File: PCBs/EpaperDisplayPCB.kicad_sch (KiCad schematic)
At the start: 25 parts, among them J1 Conn_01x12_FPC_0.5mm, J2 Conn_01x08, Q1 AO3404A, U1 ePaper-2.66

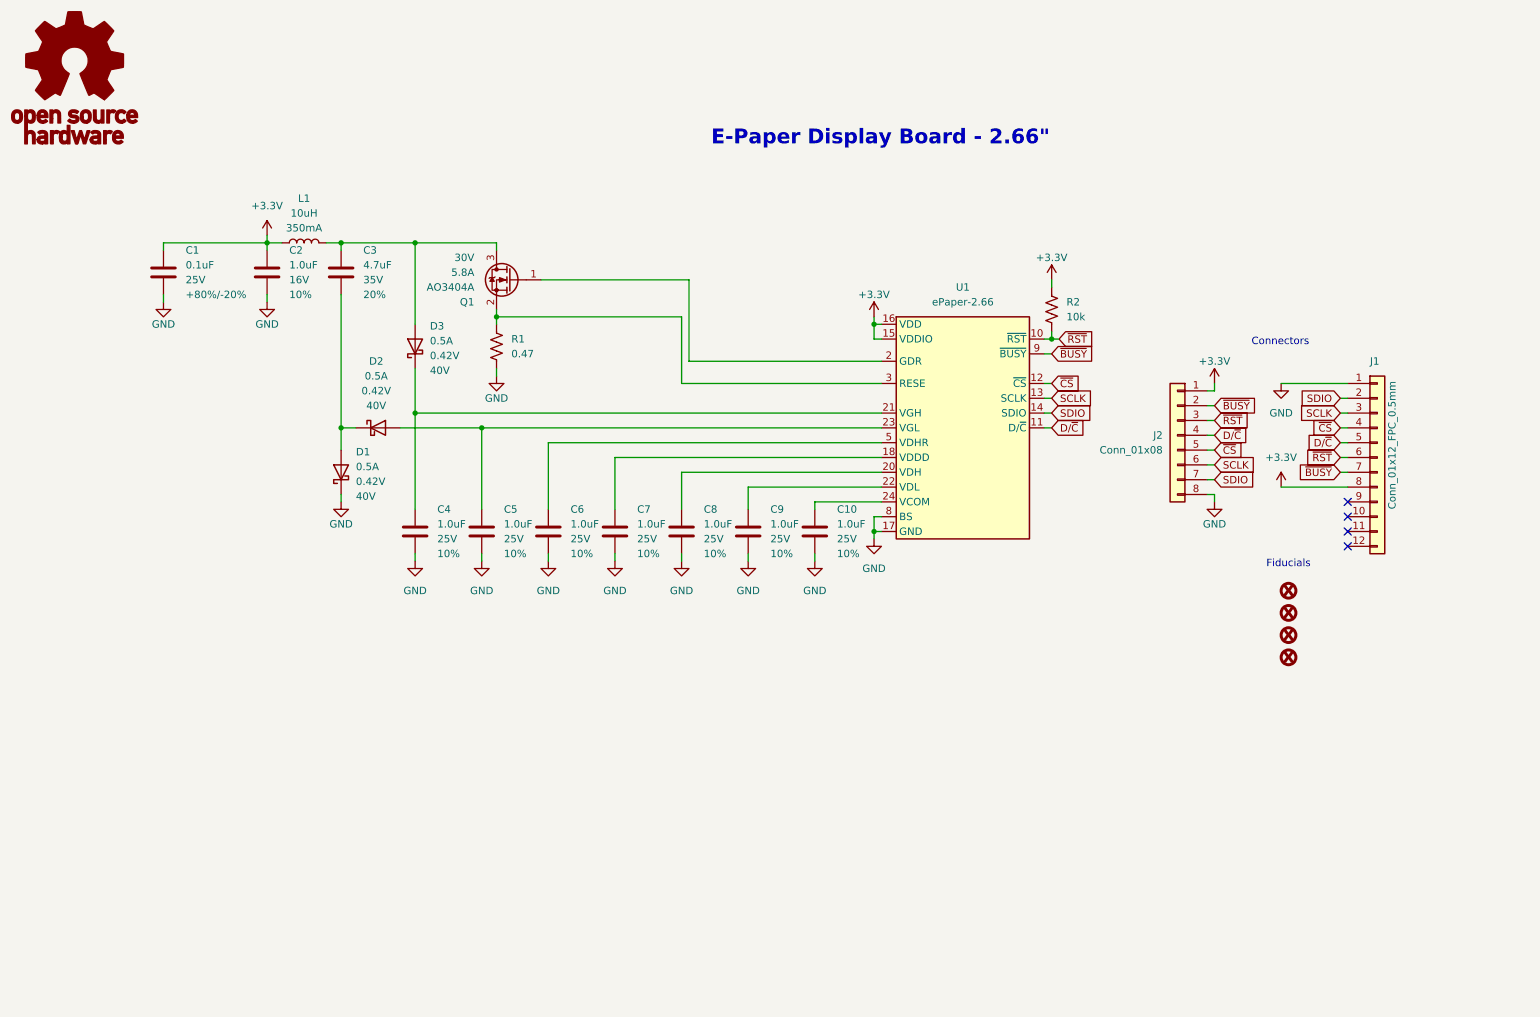
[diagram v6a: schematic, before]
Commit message: Screen and Main Board Updates
Updated Main board to Screen PCB connection, added accelerometer to Epaper display PCB. Removed GPIO 0 PB and replaced external Reset button with GPIO0 button.
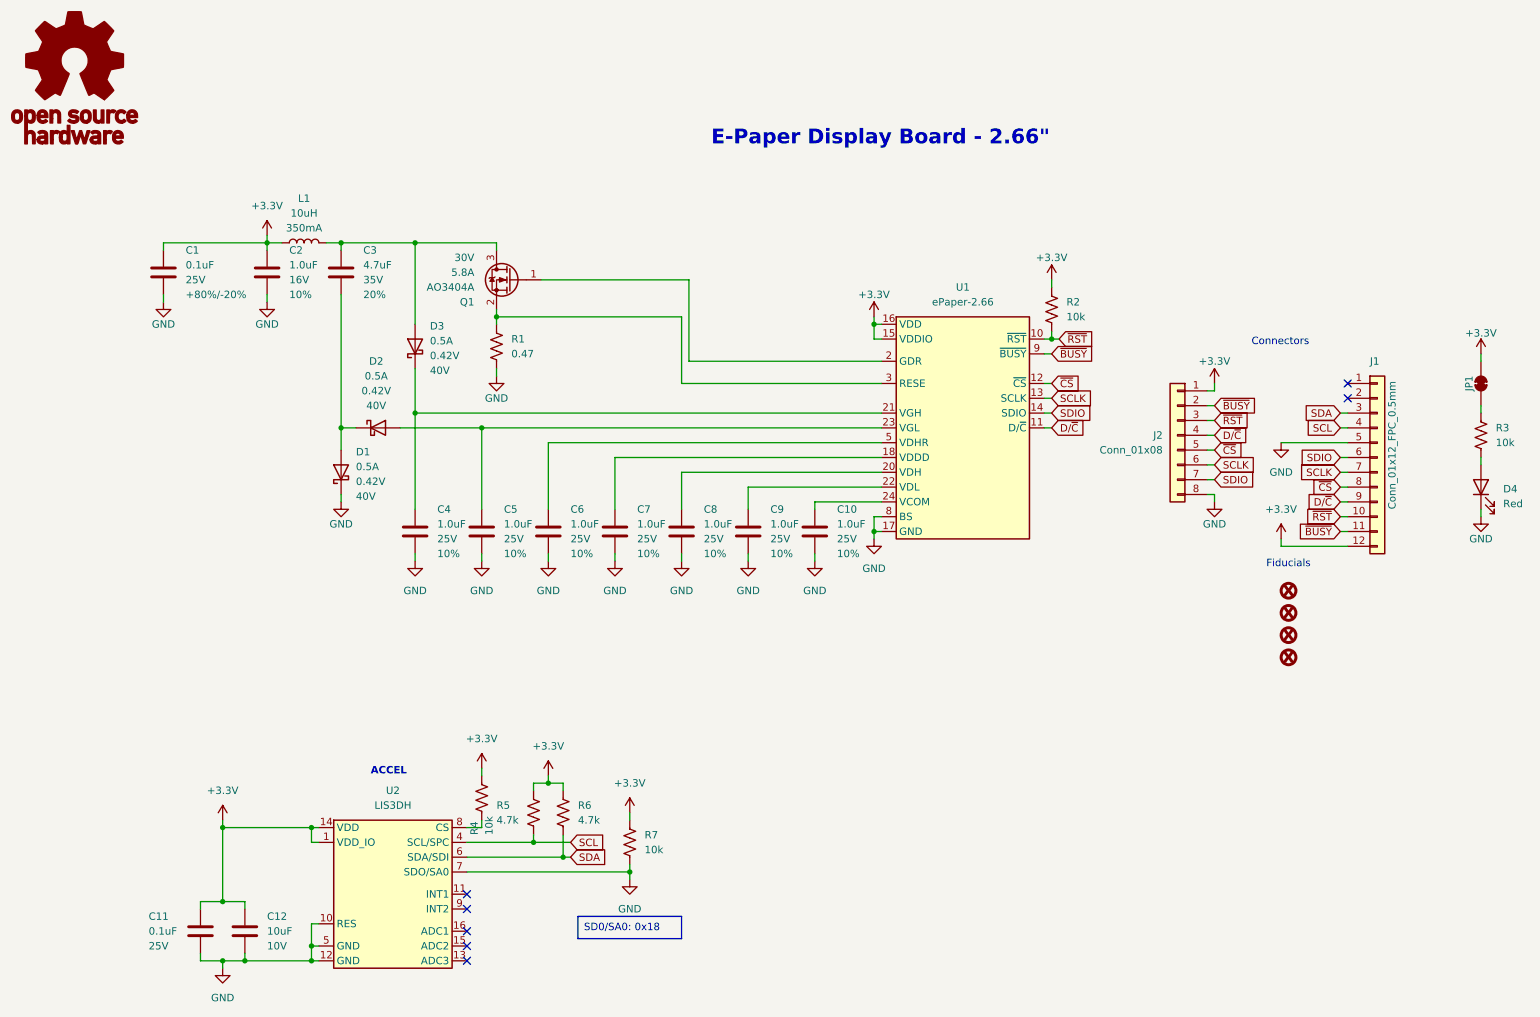
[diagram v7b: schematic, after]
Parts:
- added C11: 0.1uF, SparkFun-Capacitor:C_0603_1608Metric, symbol SparkFun-Capacitor:0.1uF_0603_25V_20%
- added C12: 10uF, SparkFun-Capacitor:C_0603_1608Metric, symbol SparkFun-Capacitor:10uF_0603_10V_20%
- added D4: Red, SparkFun-LED:LED_0603_1608Metric, symbol SparkFun-LED:LED_Red_0603
- added JP1: ~, SparkFun-Jumper:SMT-JUMPER_2_NC_TRACE_SILK, symbol SparkFun-Jumper:SolderJumper_2_Bridged
- added R3, R4, R7: 10k, SparkFun-Resistor:R_0603_1608Metric, symbol SparkFun-Resistor:10k_0603
- added R5, R6: 4.7k, SparkFun-Resistor:R_0603_1608Metric, symbol SparkFun-Resistor:4.7k_0603
- added U2: LIS3DH, Package_LGA:LGA-16_3x3mm_P0.5mm_LayoutBorder3x5y, symbol SparkFun-Sensor:LIS3DH
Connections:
- net +3.3V: now also J1.12 (Pin_12), C11.1, C12.1, JP1.2 (B), R4.2, R5.1, R6.1, R7.2, U2.1 (VDD_IO), U2.14 (VDD); no longer J1.8 (Pin_8)
- net D/~{C}: now also J1.9 (Pin_9); no longer J1.5 (Pin_5)
- net GND: now also J1.5 (Pin_5), C11.2, C12.2, D4.1 (K), R7.1, U2.10 (RES), U2.12 (GND), U2.5 (GND), U2.7 (SDO/SA0); no longer J1.1 (Pin_1)
- net SCLK: now also J1.7 (Pin_7); no longer J1.3 (Pin_3)
- net SDIO: now also J1.6 (Pin_6); no longer J1.2 (Pin_2)
- net ~{BUSY}: now also J1.11 (Pin_11); no longer J1.7 (Pin_7)
- net ~{CS}: now also J1.8 (Pin_8); no longer J1.4 (Pin_4)
- net ~{RST}: now also J1.10 (Pin_10); no longer J1.6 (Pin_6)
- new net: JP1.1 (A), R3.2
- new net: R4.1, U2.8 (CS)
- new net: D4.2 (A), R3.1
- new net SCL: J1.4 (Pin_4), R5.2, U2.4 (SCL/SPC)
- new net SDA: J1.3 (Pin_3), R6.2, U2.6 (SDA/SDI)
- no-connect marks 4 -> 7
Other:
- note added: "ACCEL"

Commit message: Adding updates From review
Fixed epaper to main board FPC connection.
Added fiducials to main board for stencil alignment purposes.
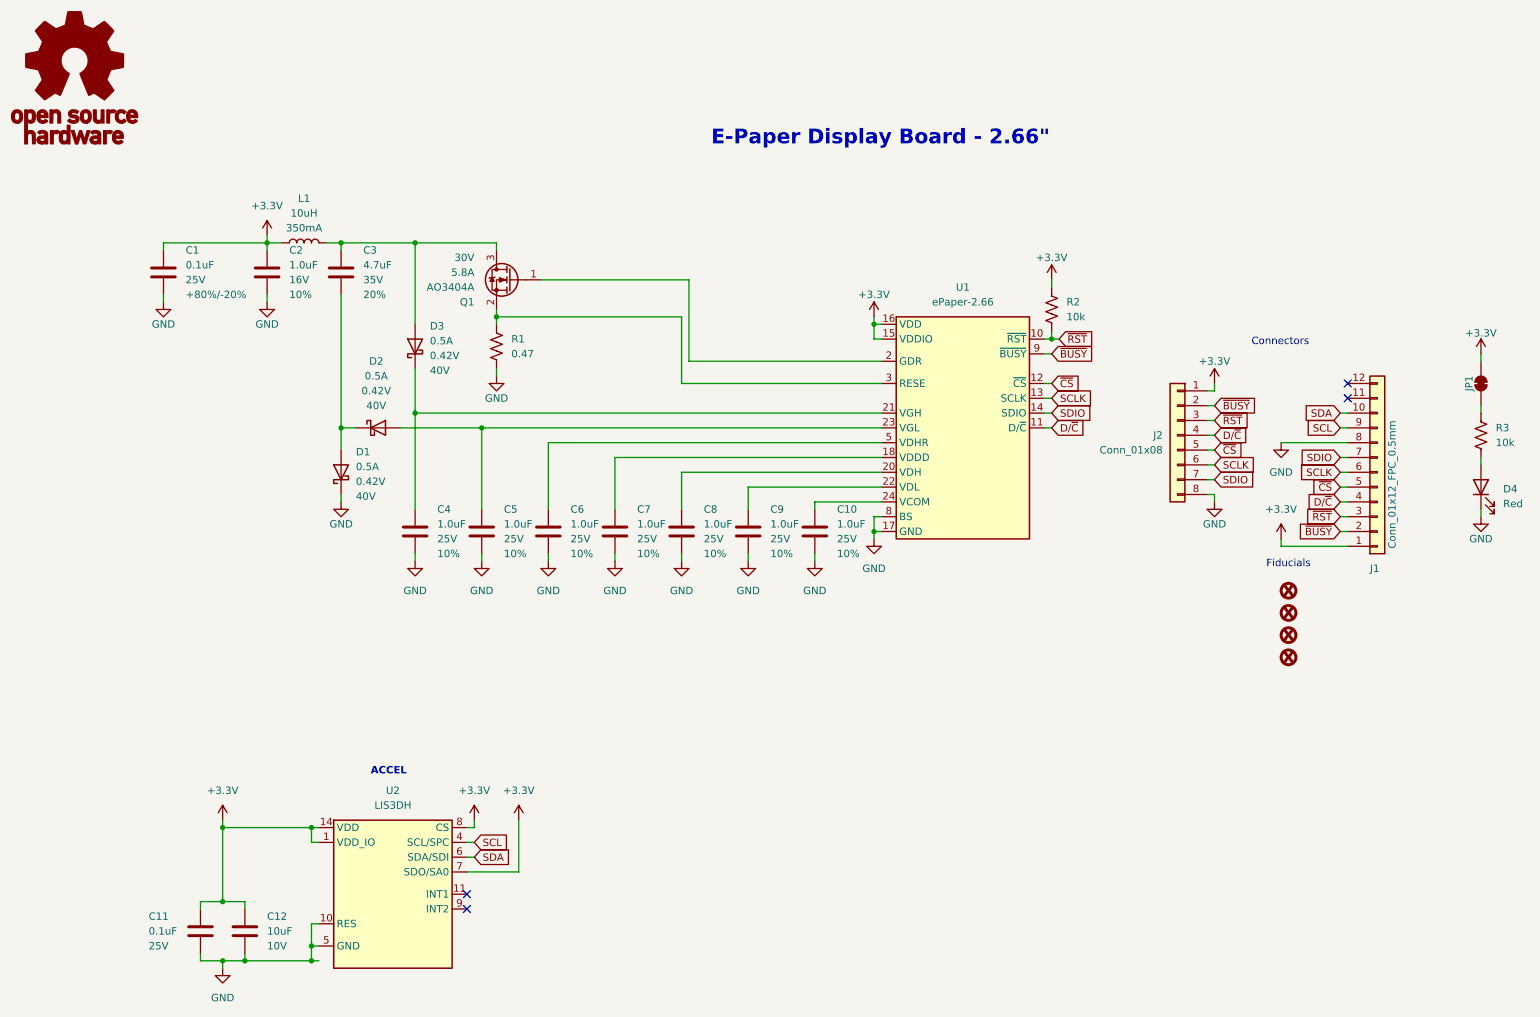
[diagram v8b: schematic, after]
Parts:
- removed R4, R7: 10k, SparkFun-Resistor:R_0603_1608Metric, symbol SparkFun-Resistor:10k_0603
- removed R5, R6: 4.7k, SparkFun-Resistor:R_0603_1608Metric, symbol SparkFun-Resistor:4.7k_0603
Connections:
- net +3.3V: now also J1.1 (Pin_1), U2.7 (SDO/SA0), U2.8 (CS); no longer J1.12 (Pin_12)
- net D/~{C}: now also J1.4 (Pin_4); no longer J1.9 (Pin_9)
- net GND: now also J1.8 (Pin_8); no longer J1.5 (Pin_5), U2.7 (SDO/SA0)
- net SCL: now also J1.9 (Pin_9); no longer J1.4 (Pin_4)
- net SCLK: now also J1.6 (Pin_6); no longer J1.7 (Pin_7)
- net SDA: now also J1.10 (Pin_10); no longer J1.3 (Pin_3)
- net SDIO: now also J1.7 (Pin_7); no longer J1.6 (Pin_6)
- net ~{BUSY}: now also J1.2 (Pin_2); no longer J1.11 (Pin_11)
- net ~{CS}: now also J1.5 (Pin_5); no longer J1.8 (Pin_8)
- net ~{RST}: now also J1.3 (Pin_3); no longer J1.10 (Pin_10)
- no-connect marks 7 -> 4
